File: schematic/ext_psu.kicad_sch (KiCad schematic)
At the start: 2 parts, among them J3 Conn_01x04, J4 DIN-5_180degree

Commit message: added pdf schematic, cleanup pdf files, added 3D image, updated readme
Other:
- title: Reverse Engineer Colecovision -> Righteous Tentacle, Colecovision Reverse Engineering Project
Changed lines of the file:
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@@
   (paper "USLetter")
   (title_block
-    (title "Reverse Engineer Colecovision")
+    (title "Righteous Tentacle, Colecovision Reverse Engineering Project")
     (date "2023-03-14")
     (rev "DEV")

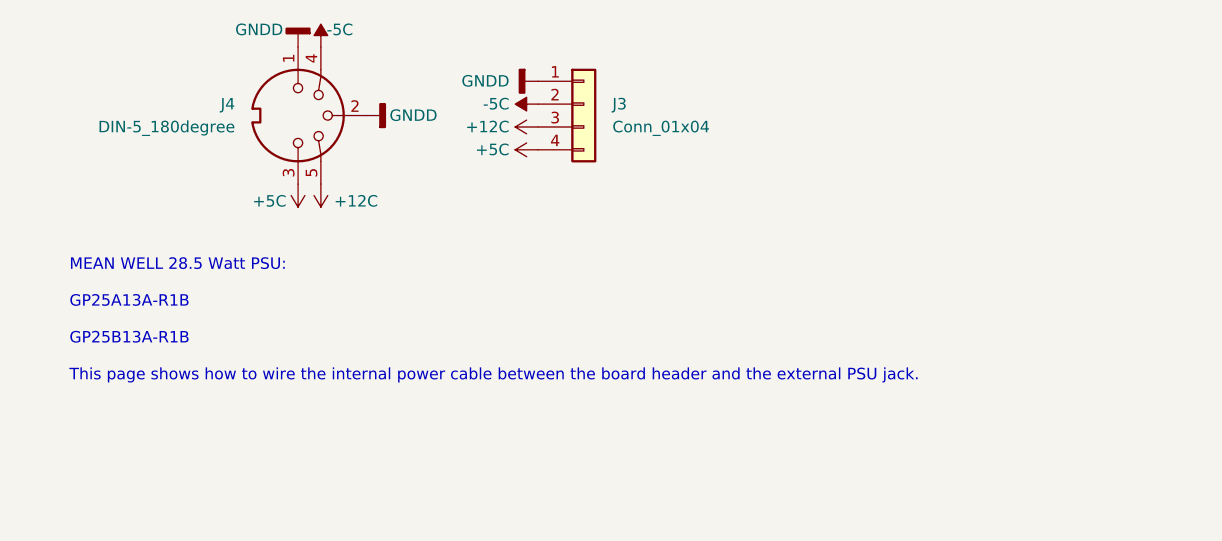
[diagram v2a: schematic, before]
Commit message: added new power supply info
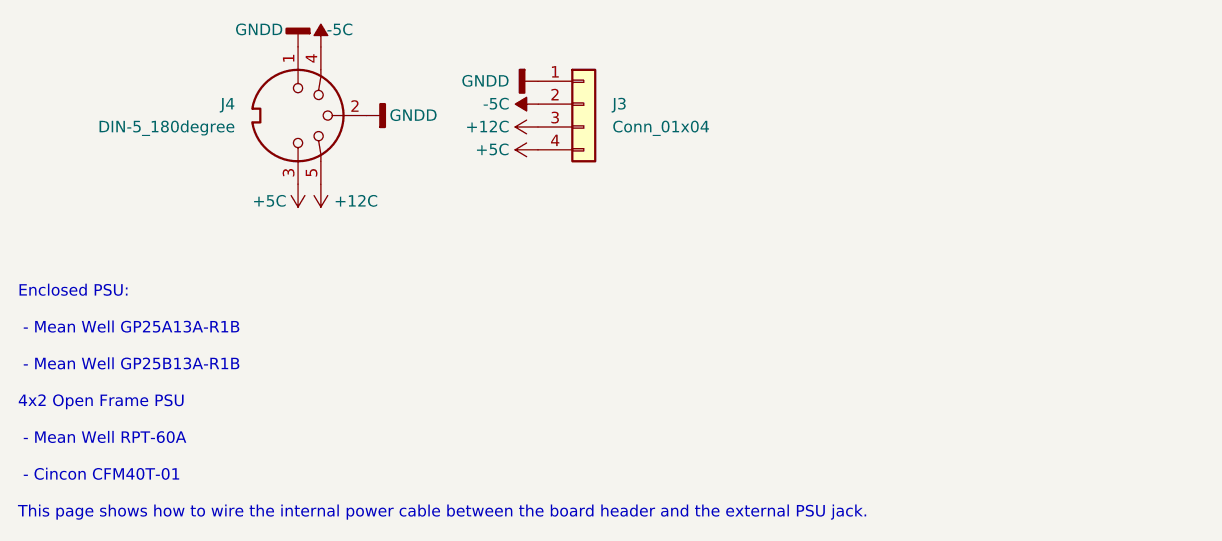
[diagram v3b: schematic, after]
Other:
- note added: "Enclosed PSU: - Mean Well GP25A13A-R1B - Mean Well GP25B13A-R1B 4x2 Open Frame PSU - Mean Well RPT-60A - Cincon CFM40T-01 This page shows how to wire the internal power cable between the board header and the external PSU jack."
- note removed: "MEAN WELL 28.5 Watt PSU: GP25A13A-R1B GP25B13A-R1B This page shows how to wire the internal power cable between the board header and the external PSU jack."
